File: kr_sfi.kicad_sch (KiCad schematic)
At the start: 91 parts, among them U11 TLK10232CTR, U12 TPS3840PL30DBVR, U13 NTS0102_TSSOP, U18 74AUP2G132, Y2 Oscillator_156.25MHz_SG3225EEN

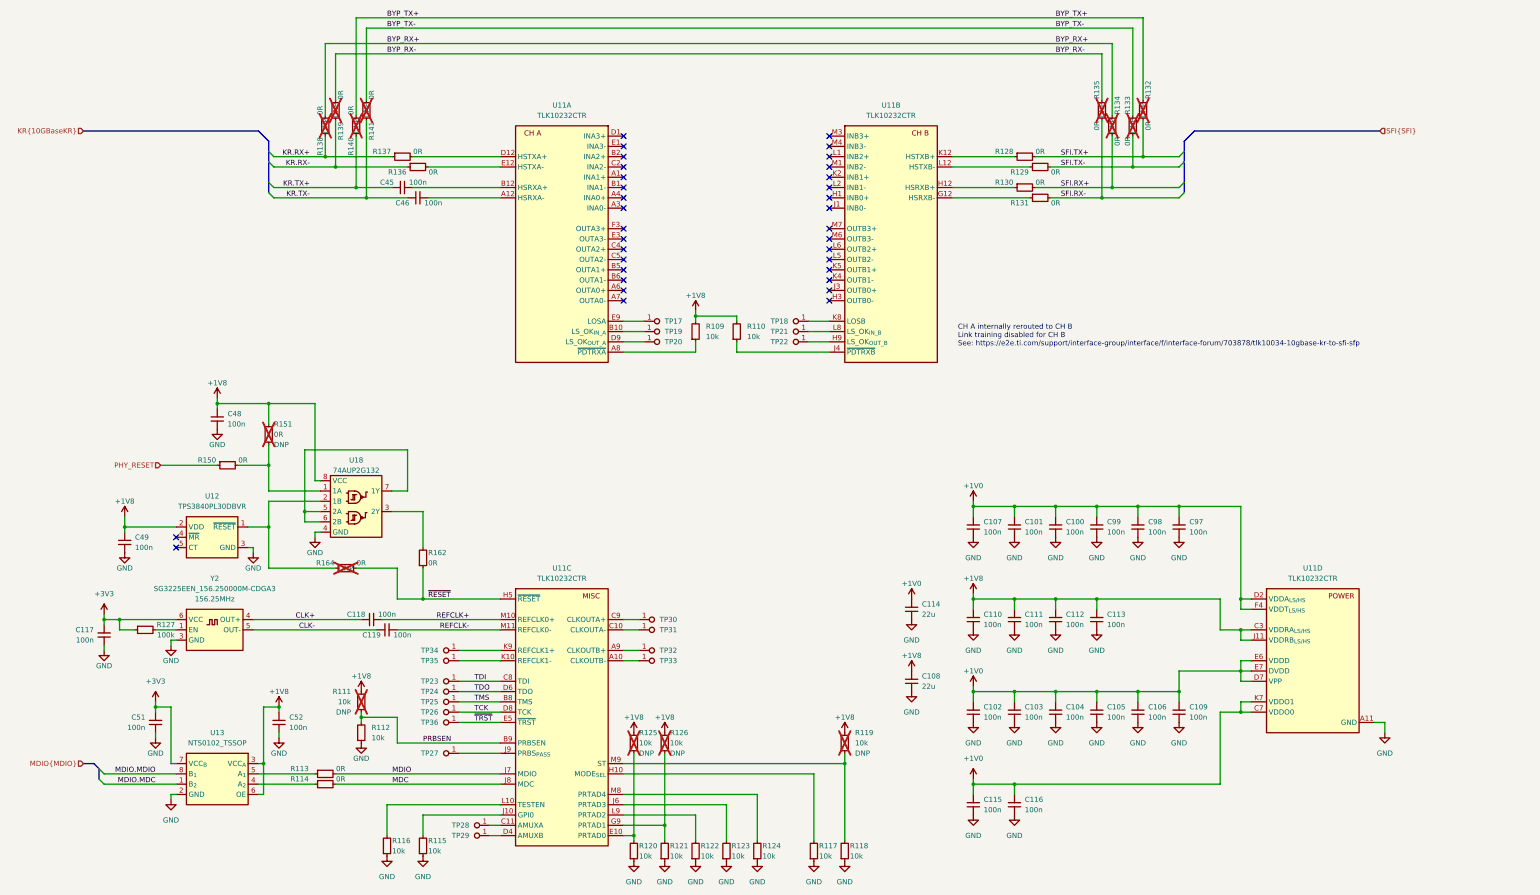
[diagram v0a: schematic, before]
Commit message: [#58137] Update backplane connector pinout
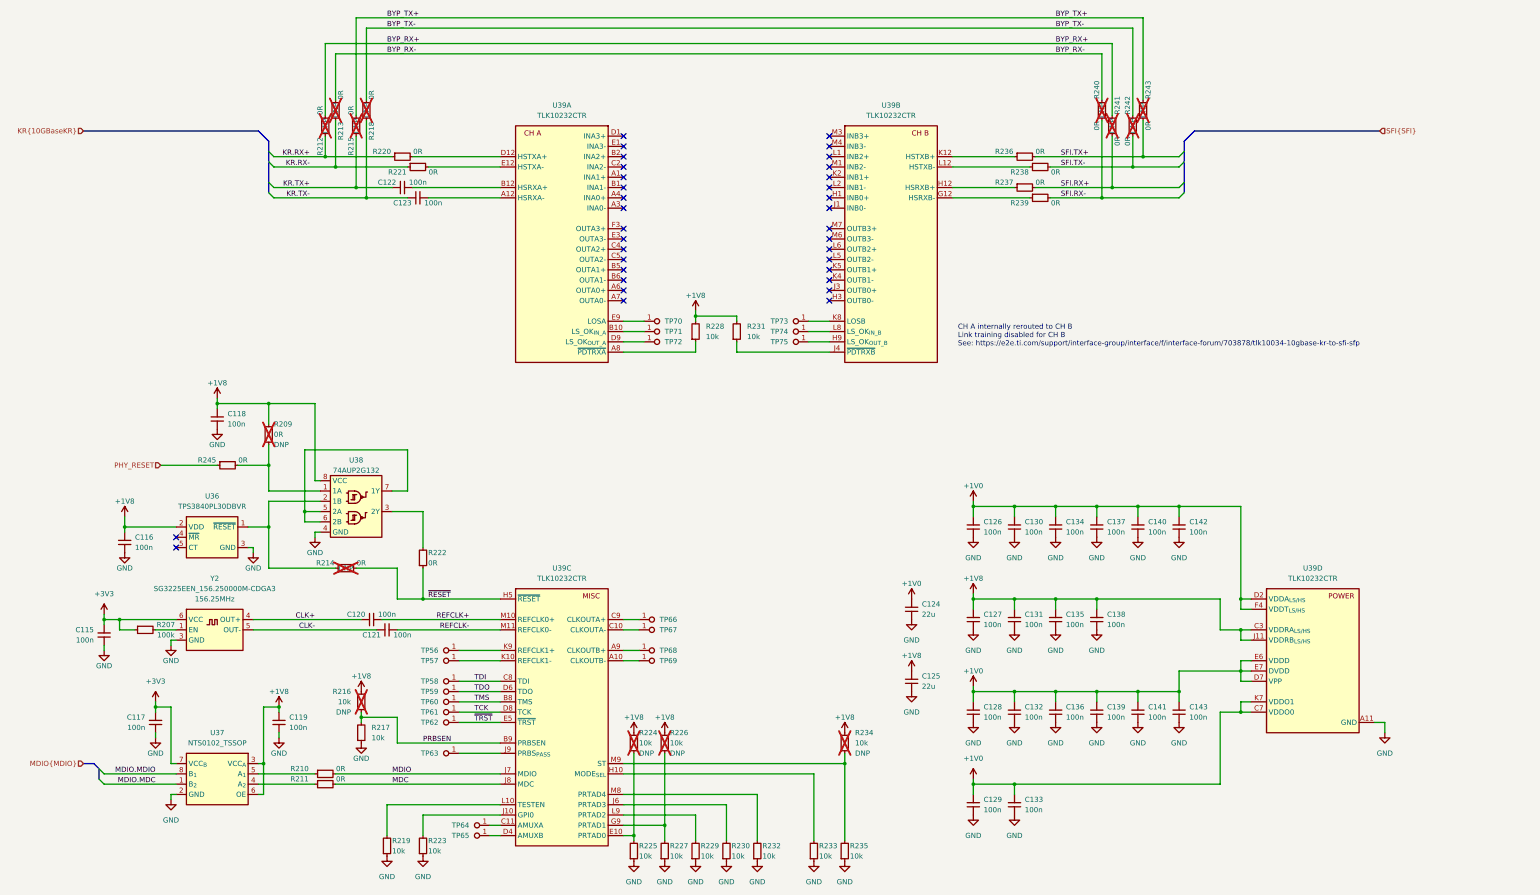
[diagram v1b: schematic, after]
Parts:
- renumbered C117 to C115, C49 to C116, C51 to C117, C48 to C118, C52 to C119, C118 to C120, C119 to C121, C45 to C122, C46 to C123, C114 to C124, C108 to C125, C107 to C126, C110 to C127, C102 to C128, C115 to C129, C101 to C130, C111 to C131, C103 to C132, C116 to C133, C100 to C134, C112 to C135, C104 to C136, C99 to C137, C113 to C138, C105 to C139, C98 to C140, C106 to C141, C97 to C142, C109 to C143, R127 to R207, R151 to R209, R113 to R210, R114 to R211, R138 to R212, R139 to R213, R164 to R214, R140 to R215, R111 to R216, R112 to R217, R141 to R218, R116 to R219, R137 to R220, R136 to R221, R162 to R222, R115 to R223, R125 to R224, R120 to R225, R126 to R226, R121 to R227, R109 to R228, R122 to R229, R123 to R230, R110 to R231, R124 to R232, R117 to R233, R119 to R234, R118 to R235, R128 to R236, R130 to R237, R129 to R238, R131 to R239, R135 to R240, R134 to R241, R133 to R242, R132 to R243, R150 to R245, TP34 to TP56, TP35 to TP57, TP23 to TP58, TP24 to TP59, TP25 to TP60, TP26 to TP61, TP36 to TP62, TP27 to TP63, TP28 to TP64, TP29 to TP65, TP30 to TP66, TP31 to TP67, TP32 to TP68, TP33 to TP69, TP17 to TP70, TP19 to TP71, TP20 to TP72, TP18 to TP73, TP21 to TP74, TP22 to TP75, U12 to U36, U13 to U37, U18 to U38, U11 to U39

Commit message: Update symbols from the library
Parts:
- U39: footprint (none) -> antmicro-footprints:BGA-144_12x12_13.05x13.05mm_P1.0mm
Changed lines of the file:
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@@
       (effects (font (size 1.27 1.27) (thickness 0.15)) (justify left bottom) hide)
     )
-    (property "Footprint" "" (at 288.29 83.82 0)
+    (property "Footprint" "antmicro-footprints:BGA-144_12x12_13.05x13.05mm_P1.0mm" (at 288.29 83.82 0)
       (effects (font (size 1.27 1.27) (thickness 0.15)) (justify left bottom) hide)
     )
@@
       (effects (font (size 1.27 1.27) (thickness 0.15)) (justify left bottom) hide)
     )
-    (property "Footprint" "" (at 207.01 198.12 0)
+    (property "Footprint" "antmicro-footprints:BGA-144_12x12_13.05x13.05mm_P1.0mm" (at 207.01 198.12 0)
       (effects (font (size 1.27 1.27) (thickness 0.15)) (justify left bottom) hide)
     )
@@
     )
   )
-  (symbol (lib_name "TLK10232CTR_1") (lib_id "antmicroInterfaceControllers:TLK10232CTR") (at 345.44 185.42 0) (unit 4)
+  (symbol (lib_id "antmicroInterfaceControllers:TLK10232CTR") (at 345.44 185.42 0) (unit 4)
     (in_bom yes) (on_board yes) (dnp no) (fields_autoplaced)
     (property "Reference" "U39" (at 360.68 177.8 0)
@@
       (effects (font (size 1.27 1.27) (thickness 0.15)) (justify left bottom) hide)
     )
-    (property "Footprint" "" (at 392.43 198.12 0)
+    (property "Footprint" "antmicro-footprints:BGA-144_12x12_13.05x13.05mm_P1.0mm" (at 392.43 198.12 0)
       (effects (font (size 1.27 1.27) (thickness 0.15)) (justify left bottom) hide)
     )
@@
       (effects (font (size 1.27 1.27) (thickness 0.15)) (justify left bottom) hide)
     )
-    (property "Footprint" "" (at 143.51 83.82 0)
-      (effects (font (size 1.27 1.27) (thickness 0.15)) (justify left bottom) hide)
-    )
+    (property "Footprint" "antmicro-footprints:BGA-144_12x12_13.05x13.05mm_P1.0mm" (at 143.51 83.82 0)
+      (effects (font (size 1.27 1.27) (thickness 0.15)) (justify left bottom) hide)
+    )

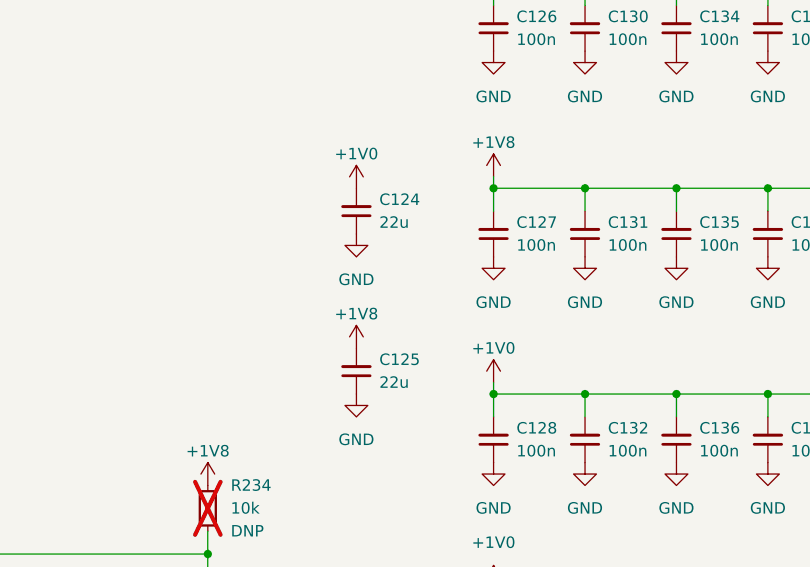
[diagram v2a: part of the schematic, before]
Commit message: [#58137] Add DC/DC supplies
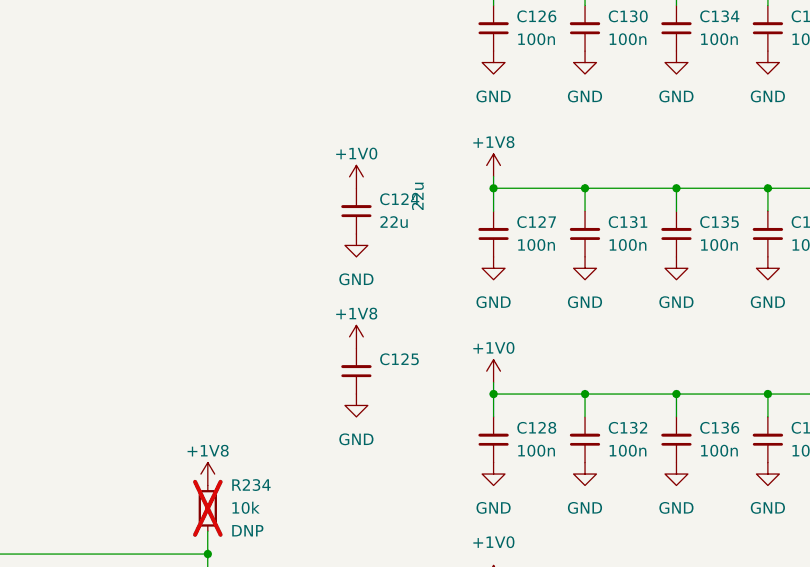
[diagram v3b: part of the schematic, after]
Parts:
- C124, C125: value C_22u_0603 -> C_22u_16V_0603; symbol antmicroCapacitors0603:C_22u_0603 -> antmicroCapacitors0603:C_22u_16V_0603; MPN GRM188R60J226MEA0D -> CL10A226MO7JZNC; Manufacturer Murata -> Samsung Electro-Mechanics; Voltage (none) -> 16V
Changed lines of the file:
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@@
     )
   )
-  (symbol (lib_id "antmicroCapacitors0603:C_22u_0603") (at 261.62 190.5 90) (unit 1)
+  (symbol (lib_id "antmicroCapacitors0603:C_22u_16V_0603") (at 261.62 190.5 90) (unit 1)
     (in_bom yes) (on_board yes) (dnp no) (fields_autoplaced)
-    (property "Reference" "C124" (at 264.16 186.6836 90)
-      (effects (font (size 1.27 1.27) (thickness 0.15)) (justify right))
-    )
-    (property "Value" "C_22u_0603" (at 271.78 170.18 0)
+    (property "Reference" "C124" (at 264.16 186.6835 90)
+      (effects (font (size 1.27 1.27) (thickness 0.15)) (justify right))
+    )
+    (property "Value" "C_22u_16V_0603" (at 271.78 170.18 0)
       (effects (font (size 1.27 1.27) (thickness 0.15)) (justify left bottom) hide)
     )
@@
       (effects (font (size 1.27 1.27) (thickness 0.15)) (justify left bottom) hide)
     )
-    (property "Datasheet" "https://www.murata.com/products/productdetail?partno=GRM188R60J226MEA0%23" (at 276.86 170.18 0)
-      (effects (font (size 1.27 1.27) (thickness 0.15)) (justify left bottom) hide)
-    )
-    (property "MPN" "GRM188R60J226MEA0D" (at 279.4 170.18 0)
-      (effects (font (size 1.27 1.27) (thickness 0.15)) (justify left bottom) hide)
-    )
-    (property "Manufacturer" "Murata" (at 281.94 170.18 0)
+    (property "Datasheet" "https://product.samsungsem.com/mlcc/CL10A226MO7JZN.do" (at 276.86 170.18 0)
+      (effects (font (size 1.27 1.27) (thickness 0.15)) (justify left bottom) hide)
+    )
+    (property "MPN" "CL10A226MO7JZNC" (at 279.4 170.18 0)
+      (effects (font (size 1.27 1.27) (thickness 0.15)) (justify left bottom) hide)
+    )
+    (property "Manufacturer" "Samsung Electro-Mechanics" (at 281.94 170.18 0)
       (effects (font (size 1.27 1.27) (thickness 0.15)) (justify left bottom) hide)
     )
@@
       (effects (font (size 1.27 1.27) (thickness 0.15)) (justify left bottom) hide)
     )
-    (property "Val" "22u" (at 264.16 189.2236 90)
-      (effects (font (size 1.27 1.27) (thickness 0.15)) (justify right))
-    )
-    (property "Voltage" "" (at 289.56 170.18 0)
+    (property "Val" "22u" (at 264.16 189.2235 90)
+      (effects (font (size 1.27 1.27) (thickness 0.15)) (justify right))
+    )
+    (property "Voltage" "16V" (at 289.56 170.18 0)
       (effects (font (size 1.27 1.27)) (justify left bottom) hide)
     )
@@
     )
   )
-  (symbol (lib_id "antmicroCapacitors0603:C_22u_0603") (at 261.62 208.28 90) (unit 1)
+  (symbol (lib_id "antmicroCapacitors0603:C_22u_16V_0603") (at 261.62 208.28 90) (unit 1)
     (in_bom yes) (on_board yes) (dnp no)
     (property "Reference" "C125" (at 264.16 204.4636 90)
       (effects (font (size 1.27 1.27) (thickness 0.15)) (justify right))
     )
-    (property "Value" "C_22u_0603" (at 271.78 187.96 0)
+    (property "Value" "C_22u_16V_0603" (at 271.78 187.96 0)
       (effects (font (size 1.27 1.27) (thickness 0.15)) (justify left bottom) hide)
     )
@@
       (effects (font (size 1.27 1.27) (thickness 0.15)) (justify left bottom) hide)
     )
-    (property "Datasheet" "https://www.murata.com/products/productdetail?partno=GRM188R60J226MEA0%23" (at 276.86 187.96 0)
-      (effects (font (size 1.27 1.27) (thickness 0.15)) (justify left bottom) hide)
-    )
-    (property "MPN" "GRM188R60J226MEA0D" (at 279.4 187.96 0)
-      (effects (font (size 1.27 1.27) (thickness 0.15)) (justify left bottom) hide)
-    )
-    (property "Manufacturer" "Murata" (at 281.94 187.96 0)
+    (property "Datasheet" "https://product.samsungsem.com/mlcc/CL10A226MO7JZN.do" (at 276.86 187.96 0)
+      (effects (font (size 1.27 1.27) (thickness 0.15)) (justify left bottom) hide)
+    )
+    (property "MPN" "CL10A226MO7JZNC" (at 279.4 187.96 0)
+      (effects (font (size 1.27 1.27) (thickness 0.15)) (justify left bottom) hide)
+    )
+    (property "Manufacturer" "Samsung Electro-Mechanics" (at 281.94 187.96 0)
       (effects (font (size 1.27 1.27) (thickness 0.15)) (justify left bottom) hide)
     )
@@
       (effects (font (size 1.27 1.27) (thickness 0.15)) (justify left bottom) hide)
     )
-    (property "Val" "22u" (at 264.16 207.0036 90)
-      (effects (font (size 1.27 1.27) (thickness 0.15)) (justify right))
-    )
-    (property "Voltage" "" (at 289.56 187.96 0)
-      (effects (font (size 1.27 1.27)) (justify left bottom) hide)
-    )
+    (property "Val" "22u" (at 269.24 187.96 0)
+      (effects (font (size 1.27 1.27) (thickness 0.15)) (justify left bottom))
+    )
+    (property "Voltage" "16V" (at 289.56 187.96 0)
+      (effects (font (size 1.27 1.27)) (justify left bottom) hide)
+    )

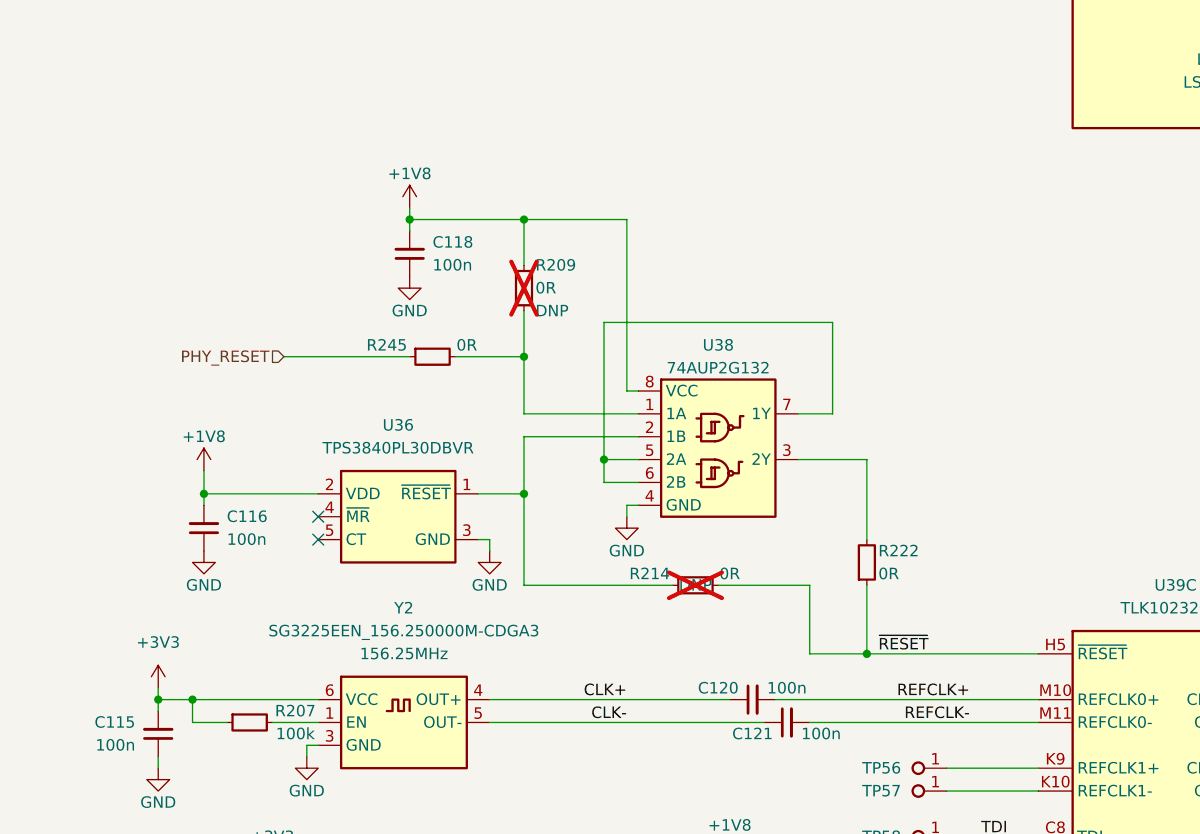
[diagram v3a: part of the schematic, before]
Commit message: [#58137] Add power sequencing and reset
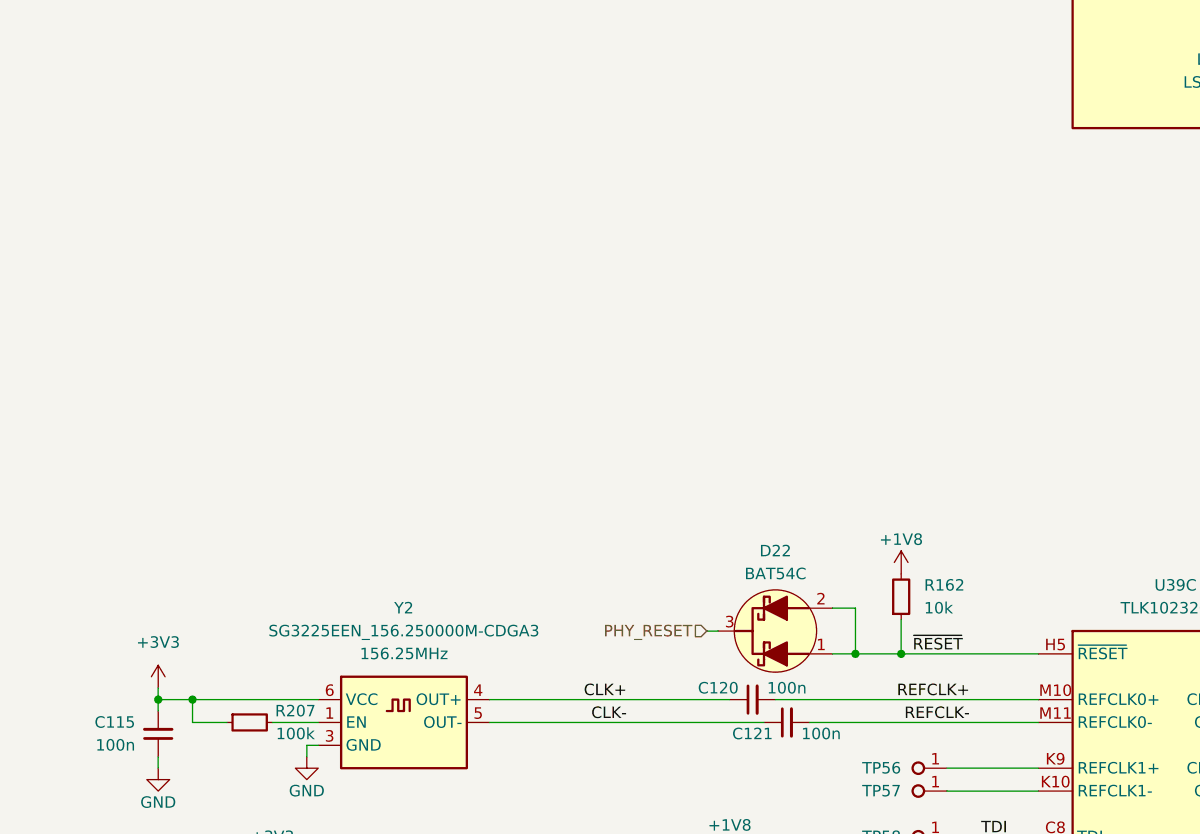
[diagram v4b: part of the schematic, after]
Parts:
- removed C116, C118: C_100n_0402, antmicro-footprints:C_0402_1005Metric, symbol antmicroCapacitors0402:C_100n_0402
- removed R209, R214, R222, R245: R_0R_0402, antmicro-footprints:R_0402_1005Metric, symbol antmicroResistors0402:R_0R_0402
- removed U36: TPS3840PL30DBVR, antmicro-footprints:SOT-23-5, symbol antmicroPMICPowerSequencers:TPS3840PL30DBVR
- removed U38: 74AUP2G132, antmicro-footprints:VSSOP-8_2.3x2mm_P0.5mm, symbol antmicroLogicGatesandInverters:74AUP2G132
- added D22: BAT54C, antmicro-footprints:SOT-23-3, symbol antmicroDiodesRectifiersSingle:BAT54C
- added R162: R_10k_0402, antmicro-footprints:R_0402_1005Metric, symbol antmicroResistors0402:R_10k_0402
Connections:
- net +1V8: now also R162.2
- net PHY_RESET: now also D22.3
- net ~{RESET}: now also D22.1, D22.2, R162.1
- no-connect marks 34 -> 32
